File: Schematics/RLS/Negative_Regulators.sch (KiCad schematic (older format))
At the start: 25 parts, among them U4 AD5293, U5 AD5293, U6 LT3015, U7 LT3015

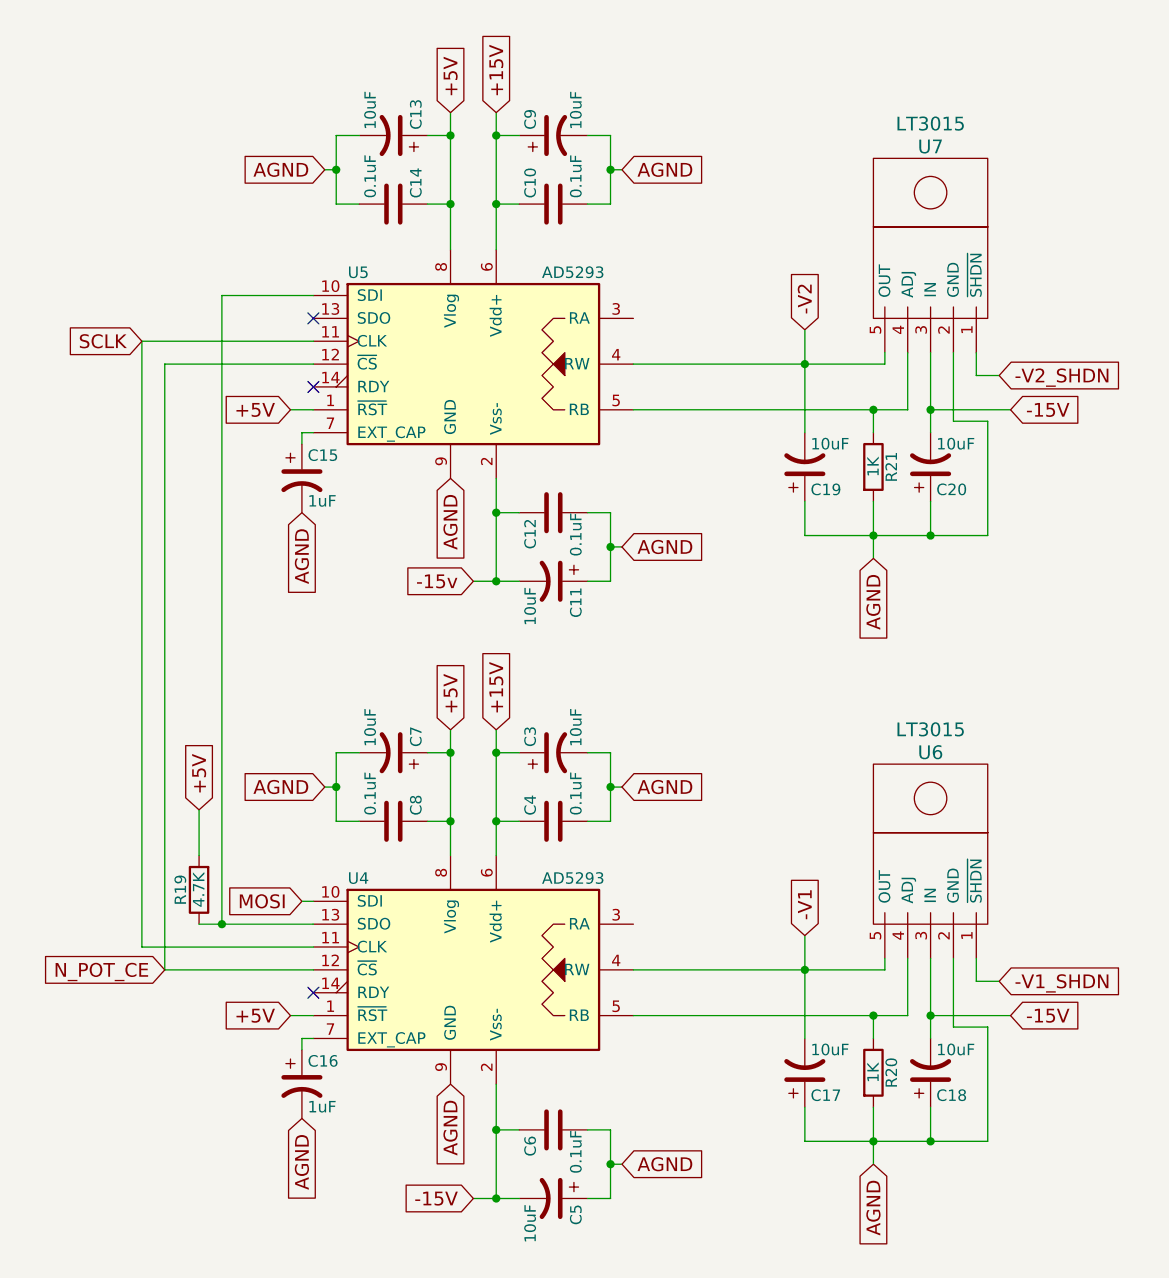
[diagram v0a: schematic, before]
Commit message: Updated Schematic (Almost Done)
Finished both variable regulator circuits, added connectors for LAs, added +/- 5 regulated circuit for DB +/- 5V (needs to be tested before PCB implementation), various renaming and labeling
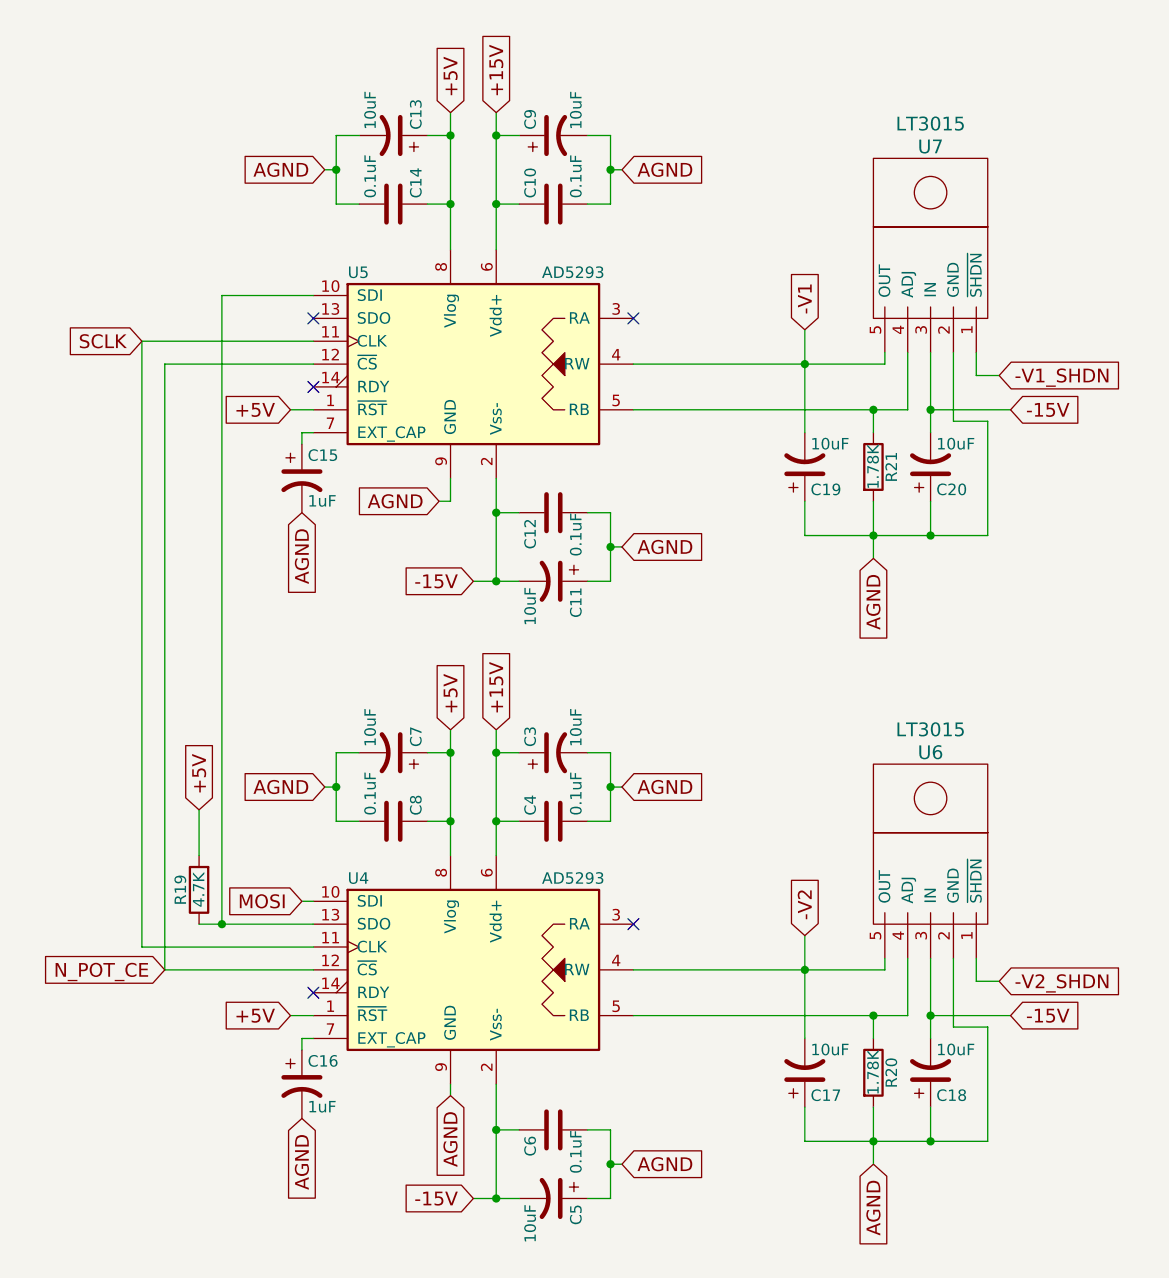
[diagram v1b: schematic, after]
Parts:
- R20, R21: value 1K -> 1.78K
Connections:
- net -15v is gone; now on net -15V: C11.2, C12.1, U5.2 (Vss-)
- net -V1: now also C19.2, U5.4 (RW), U7.5 (OUT); no longer C17.2, U4.4 (RW), U6.5 (OUT)
- net -V1_SHDN: now also U7.1 (~SHDN); no longer U6.1 (~SHDN)
- net -V2: now also C17.2, U4.4 (RW), U6.5 (OUT); no longer C19.2, U5.4 (RW), U7.5 (OUT)
- net -V2_SHDN: now also U6.1 (~SHDN); no longer U7.1 (~SHDN)
- no-connect marks 3 -> 5
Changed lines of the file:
@@
 $Descr A4 11693 8268
 encoding utf-8
-Sheet 4 5
+Sheet 4 7
 Title ""
 Date ""
@@
 Text GLabel 3400 1200 0    60   Input ~ 0
 AGND
-Text GLabel 3950 5200 3    60   Input ~ 0
-AGND
-Text GLabel 3950 2550 3    60   Input ~ 0
+Text GLabel 3950 5250 3    60   Input ~ 0
+AGND
+Text GLabel 3900 2650 0    60   Input ~ 0
 AGND
 $Comp
@@
 AGND
 Text GLabel 4050 3000 0    60   Input ~ 0
--15v
+-15V
 $Comp
 L CP1 C5
@@
 P 5800 5150
 F 0 "R20" V 5880 5150 50  0000 C CNN
-F 1 "1K" V 5800 5150 50  0000 C CNN
+F 1 "1.78K" V 5800 5150 50  0000 C CNN
 F 2 "" V 5730 5150 50  0001 C CNN
 F 3 "" H 5800 5150 50  0001 C CNN
@@
 $EndComp
 Text GLabel 6350 4750 2    60   Input ~ 0
--V1_SHDN
+-V2_SHDN
 Text GLabel 5800 5550 3    60   Input ~ 0
 AGND
@@
 -15V
 Text GLabel 5500 4550 1    60   Input ~ 0
--V1
+-V2
 $Comp
 L LT3015 U7
@@
 P 5800 2500
 F 0 "R21" V 5880 2500 50  0000 C CNN
-F 1 "1K" V 5800 2500 50  0000 C CNN
+F 1 "1.78K" V 5800 2500 50  0000 C CNN
 F 2 "" V 5730 2500 50  0001 C CNN
 F 3 "" H 5800 2500 50  0001 C CNN
@@
 $EndComp
 Text GLabel 6350 2100 2    60   Input ~ 0
--V2_SHDN
+-V1_SHDN
 Text GLabel 5800 2900 3    60   Input ~ 0
 AGND
@@
 -15V
 Text GLabel 5500 1900 1    60   Input ~ 0
--V2
+-V1
 Wire Wire Line
 	3350 5000 3300 5000
@@
 	4650 2700 4550 2700
 Wire Wire Line
-	4050 3000 4250 3000
-Wire Wire Line
 	4250 2700 4150 2700
-Connection ~ 4150 2700
 Wire Wire Line
 	4700 2850 4650 2850
 Connection ~ 4650 2850
-Connection ~ 4150 3000
-Wire Wire Line
-	4150 2550 4150 3000
 Wire Wire Line
 	4650 5700 4550 5700
@@
 	6400 4900 6050 4900
 Connection ~ 6050 4900
+NoConn ~ 4750 1850
+NoConn ~ 4750 4500
+Wire Wire Line
+	3950 5200 3950 5250
+Wire Wire Line
+	4050 3000 4250 3000
+Wire Wire Line
+	4150 2550 4150 3000
+Connection ~ 4150 3000
+Connection ~ 4150 2700
+Wire Wire Line
+	3900 2650 3950 2650
+Wire Wire Line
+	3950 2650 3950 2550
 $EndSCHEMATC

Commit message: Most Footprints Added
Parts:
- C10, C12, C14, C4, C6, C8: footprint (none) -> Capacitors_SMD:C_0603_HandSoldering
- C11, C13, C15, C16, C17, C18, C19, C20, C3, C5, C7, C9: footprint (none) -> Capacitors_SMD:CP_Elec_4x5.3
- R19: footprint (none) -> Resistors_SMD:R_0805_HandSoldering
- R20, R21: footprint (none) -> Resistors_SMD:R_1206_HandSoldering
- U4, U5: footprint (none) -> SMD_Packages:SSOP-14
- U6, U7: footprint (none) -> TO_SOT_Packages_THT:TO-220-5_Pentawatt_Multiwatt-5_Vertical_StaggeredType1
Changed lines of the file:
@@
 F 0 "U6" H 6150 4750 60  0000 C CNN
 F 1 "LT3015" H 6150 4850 60  0000 C CNN
-F 2 "" H 6150 4750 60  0001 C CNN
+F 2 "TO_SOT_Packages_THT:TO-220-5_Pentawatt_Multiwatt-5_Vertical_StaggeredType1" H 6150 4750 60  0001 C CNN
 F 3 "" H 6150 4750 60  0001 C CNN
 	1    6100 4250
@@
 F 0 "U4" H 3500 5100 50  0000 L CNN
 F 1 "AD5293" H 4350 5100 50  0000 L CNN
-F 2 "" H 4050 4700 50  0001 C CNN
+F 2 "SMD_Packages:SSOP-14" H 4050 4700 50  0001 C CNN
 F 3 "" H 4050 4700 50  0001 C CNN
 	1    4050 4700
@@
 F 0 "U5" H 3500 2450 50  0000 L CNN
 F 1 "AD5293" H 4350 2450 50  0000 L CNN
-F 2 "" H 4050 2050 50  0001 C CNN
+F 2 "SMD_Packages:SSOP-14" H 4050 2050 50  0001 C CNN
 F 3 "" H 4050 2050 50  0001 C CNN
 	1    4050 2050
@@
 F 0 "C15" H 3325 2650 50  0000 L CNN
 F 1 "1uF" H 3325 2450 50  0000 L CNN
-F 2 "" H 3300 2550 50  0001 C CNN
+F 2 "Capacitors_SMD:CP_Elec_4x5.3" H 3300 2550 50  0001 C CNN
 F 3 "" H 3300 2550 50  0001 C CNN
 	1    3300 2550
@@
 F 0 "C16" H 3325 5300 50  0000 L CNN
 F 1 "1uF" H 3325 5100 50  0000 L CNN
-F 2 "" H 3300 5200 50  0001 C CNN
+F 2 "Capacitors_SMD:CP_Elec_4x5.3" H 3300 5200 50  0001 C CNN
 F 3 "" H 3300 5200 50  0001 C CNN
 	1    3300 5200
@@
 F 0 "C3" H 4425 3850 50  0000 L CNN
 F 1 "10uF" H 4425 3650 50  0000 L CNN
-F 2 "" H 4400 3750 50  0001 C CNN
+F 2 "Capacitors_SMD:CP_Elec_4x5.3" H 4400 3750 50  0001 C CNN
 F 3 "" H 4400 3750 50  0001 C CNN
 	1    4400 3750
@@
 F 0 "C4" H 4425 4150 50  0000 L CNN
 F 1 "0.1uF" H 4425 3950 50  0000 L CNN
-F 2 "" H 4438 3900 50  0001 C CNN
+F 2 "Capacitors_SMD:C_0603_HandSoldering" H 4438 3900 50  0001 C CNN
 F 3 "" H 4400 4050 50  0001 C CNN
 	1    4400 4050
@@
 F 0 "R19" V 2930 4350 50  0000 C CNN
 F 1 "4.7K" V 2850 4350 50  0000 C CNN
-F 2 "" V 2780 4350 50  0001 C CNN
+F 2 "Resistors_SMD:R_0805_HandSoldering" V 2780 4350 50  0001 C CNN
 F 3 "" H 2850 4350 50  0001 C CNN
 	1    2850 4350
@@
 F 0 "C7" H 3725 3850 50  0000 L CNN
 F 1 "10uF" H 3725 3650 50  0000 L CNN
-F 2 "" H 3700 3750 50  0001 C CNN
+F 2 "Capacitors_SMD:CP_Elec_4x5.3" H 3700 3750 50  0001 C CNN
 F 3 "" H 3700 3750 50  0001 C CNN
 	1    3700 3750
@@
 F 0 "C8" H 3725 4150 50  0000 L CNN
 F 1 "0.1uF" H 3725 3950 50  0000 L CNN
-F 2 "" H 3738 3900 50  0001 C CNN
+F 2 "Capacitors_SMD:C_0603_HandSoldering" H 3738 3900 50  0001 C CNN
 F 3 "" H 3700 4050 50  0001 C CNN
 	1    3700 4050
@@
 F 0 "C9" H 4425 1150 50  0000 L CNN
 F 1 "10uF" H 4425 950 50  0000 L CNN
-F 2 "" H 4400 1050 50  0001 C CNN
+F 2 "Capacitors_SMD:CP_Elec_4x5.3" H 4400 1050 50  0001 C CNN
 F 3 "" H 4400 1050 50  0001 C CNN
 	1    4400 1050
@@
 F 0 "C10" H 4425 1450 50  0000 L CNN
 F 1 "0.1uF" H 4425 1250 50  0000 L CNN
-F 2 "" H 4438 1200 50  0001 C CNN
+F 2 "Capacitors_SMD:C_0603_HandSoldering" H 4438 1200 50  0001 C CNN
 F 3 "" H 4400 1350 50  0001 C CNN
 	1    4400 1350
@@
 F 0 "C13" H 3725 1150 50  0000 L CNN
 F 1 "10uF" H 3725 950 50  0000 L CNN
-F 2 "" H 3700 1050 50  0001 C CNN
+F 2 "Capacitors_SMD:CP_Elec_4x5.3" H 3700 1050 50  0001 C CNN
 F 3 "" H 3700 1050 50  0001 C CNN
 	1    3700 1050
@@
 F 0 "C14" H 3725 1450 50  0000 L CNN
 F 1 "0.1uF" H 3725 1250 50  0000 L CNN
-F 2 "" H 3738 1200 50  0001 C CNN
+F 2 "Capacitors_SMD:C_0603_HandSoldering" H 3738 1200 50  0001 C CNN
 F 3 "" H 3700 1350 50  0001 C CNN
 	1    3700 1350
@@
 F 0 "C11" H 4425 3100 50  0000 L CNN
 F 1 "10uF" H 4425 2900 50  0000 L CNN
-F 2 "" H 4400 3000 50  0001 C CNN
+F 2 "Capacitors_SMD:CP_Elec_4x5.3" H 4400 3000 50  0001 C CNN
 F 3 "" H 4400 3000 50  0001 C CNN
 	1    4400 3000
@@
 F 0 "C12" H 4425 2800 50  0000 L CNN
 F 1 "0.1uF" H 4400 2600 50  0000 L CNN
-F 2 "" H 4438 2550 50  0001 C CNN
+F 2 "Capacitors_SMD:C_0603_HandSoldering" H 4438 2550 50  0001 C CNN
 F 3 "" H 4400 2700 50  0001 C CNN
 	1    4400 2700
@@
 F 0 "C5" H 4425 5800 50  0000 L CNN
 F 1 "10uF" H 4425 5600 50  0000 L CNN
-F 2 "" H 4400 5700 50  0001 C CNN
+F 2 "Capacitors_SMD:CP_Elec_4x5.3" H 4400 5700 50  0001 C CNN
 F 3 "" H 4400 5700 50  0001 C CNN
 	1    4400 5700
@@
 F 0 "C6" H 4425 5500 50  0000 L CNN
 F 1 "0.1uF" H 4400 5300 50  0000 L CNN
-F 2 "" H 4438 5250 50  0001 C CNN
+F 2 "Capacitors_SMD:C_0603_HandSoldering" H 4438 5250 50  0001 C CNN
 F 3 "" H 4400 5400 50  0001 C CNN
 	1    4400 5400
@@
 F 0 "R20" V 5880 5150 50  0000 C CNN
 F 1 "1.78K" V 5800 5150 50  0000 C CNN
-F 2 "" V 5730 5150 50  0001 C CNN
+F 2 "Resistors_SMD:R_1206_HandSoldering" V 5730 5150 50  0001 C CNN
 F 3 "" H 5800 5150 50  0001 C CNN
 	1    5800 5150
@@
 F 0 "C17" H 5525 5250 50  0000 L CNN
 F 1 "10uF" H 5525 5050 50  0000 L CNN
-F 2 "" H 5500 5150 50  0001 C CNN
+F 2 "Capacitors_SMD:CP_Elec_4x5.3" H 5500 5150 50  0001 C CNN
 F 3 "" H 5500 5150 50  0001 C CNN
 	1    5500 5150
@@
 F 0 "C18" H 6075 5250 50  0000 L CNN
 F 1 "10uF" H 6075 5050 50  0000 L CNN
-F 2 "" H 6050 5150 50  0001 C CNN
+F 2 "Capacitors_SMD:CP_Elec_4x5.3" H 6050 5150 50  0001 C CNN
 F 3 "" H 6050 5150 50  0001 C CNN
 	1    6050 5150
@@
 F 0 "U7" H 6150 2100 60  0000 C CNN
 F 1 "LT3015" H 6150 2200 60  0000 C CNN
-F 2 "" H 6150 2100 60  0001 C CNN
+F 2 "TO_SOT_Packages_THT:TO-220-5_Pentawatt_Multiwatt-5_Vertical_StaggeredType1" H 6150 2100 60  0001 C CNN
 F 3 "" H 6150 2100 60  0001 C CNN
 	1    6100 1600
@@
 F 0 "R21" V 5880 2500 50  0000 C CNN
 F 1 "1.78K" V 5800 2500 50  0000 C CNN
-F 2 "" V 5730 2500 50  0001 C CNN
+F 2 "Resistors_SMD:R_1206_HandSoldering" V 5730 2500 50  0001 C CNN
 F 3 "" H 5800 2500 50  0001 C CNN
 	1    5800 2500
@@
 F 0 "C19" H 5525 2600 50  0000 L CNN
 F 1 "10uF" H 5525 2400 50  0000 L CNN
-F 2 "" H 5500 2500 50  0001 C CNN
+F 2 "Capacitors_SMD:CP_Elec_4x5.3" H 5500 2500 50  0001 C CNN
 F 3 "" H 5500 2500 50  0001 C CNN
 	1    5500 2500
@@
 F 0 "C20" H 6075 2600 50  0000 L CNN
 F 1 "10uF" H 6075 2400 50  0000 L CNN
-F 2 "" H 6050 2500 50  0001 C CNN
+F 2 "Capacitors_SMD:CP_Elec_4x5.3" H 6050 2500 50  0001 C CNN
 F 3 "" H 6050 2500 50  0001 C CNN
 	1    6050 2500
